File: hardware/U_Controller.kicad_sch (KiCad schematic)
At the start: 21 parts, among them J7001 Conn_01x06_Pin, J7002 Conn_ARM_JTAG_SWD_10, J7003 USB_C_Receptacle_USB2.0_16P, SW7001 SW_Wuerth_450301014042, U7001 STM32F401RBTx, U7003 USBLC6-2SC6, Y7001 Crystal_GND24

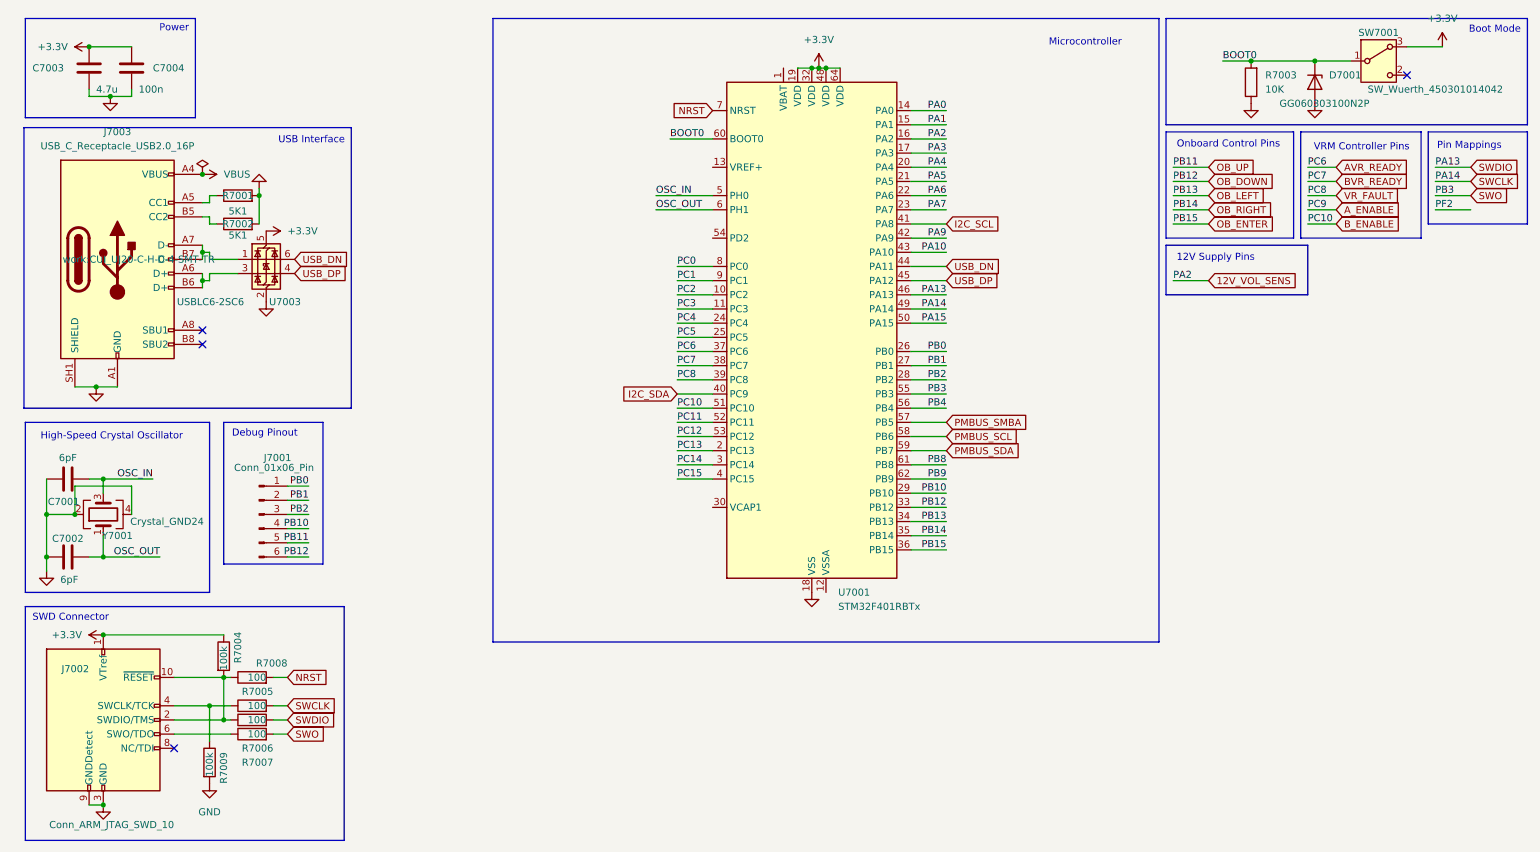
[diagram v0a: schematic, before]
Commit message: feat(schematic): refactor main heirarchy
This commit makes a bunch of changes to how power is delivered on the
schematic. It also adds the probit header and the i2c output connector
on the main page of the schematic. Lastly, it changes it so that USB
power should work and also not power the 5V rail to the mosfet ICs.
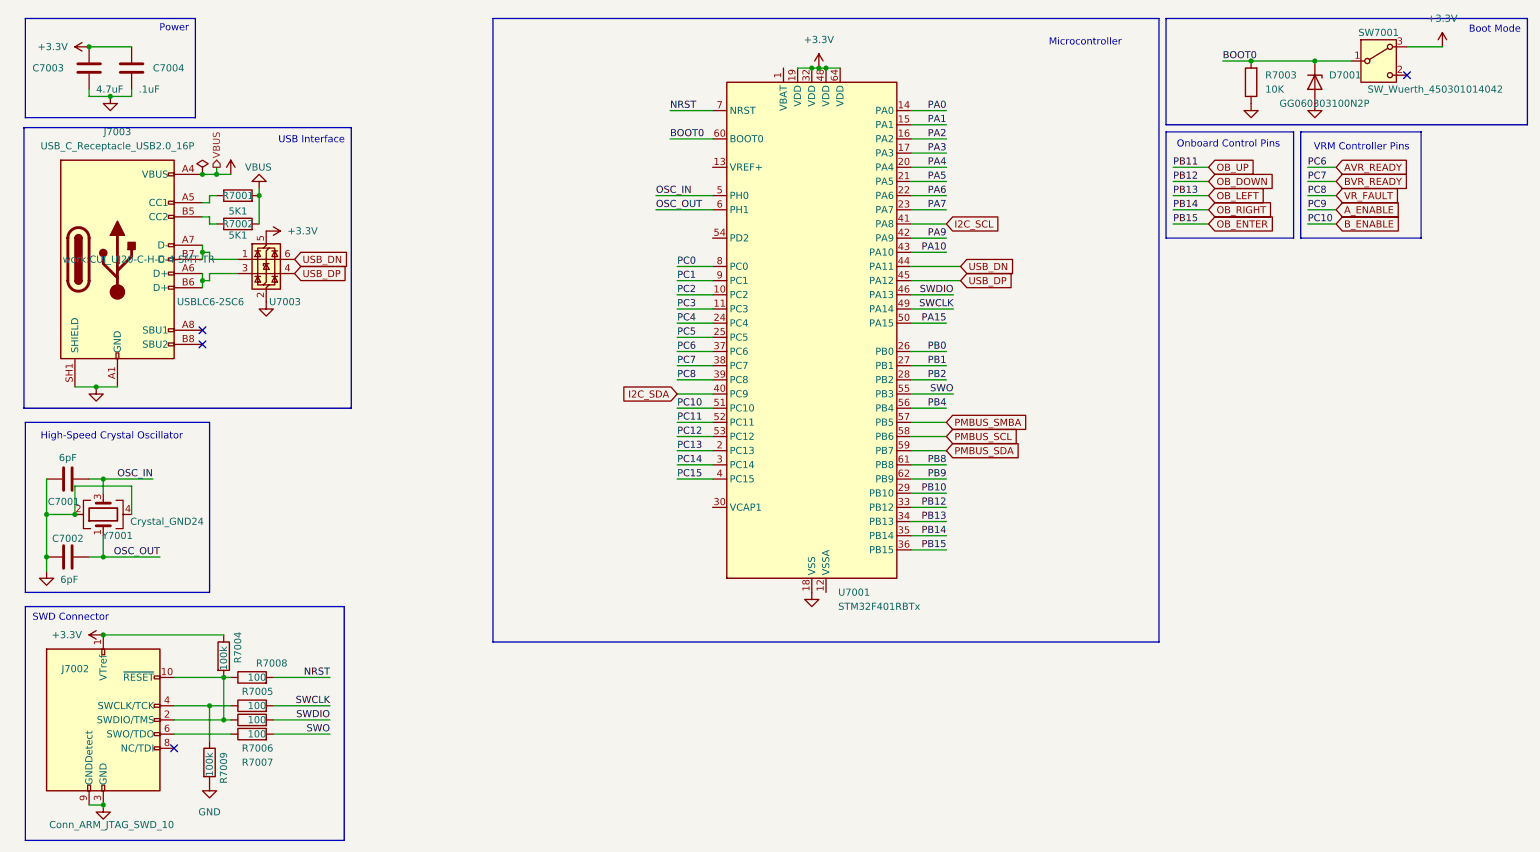
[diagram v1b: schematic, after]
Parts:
- removed J7001: Conn_01x06_Pin, symbol Connector:Conn_01x06_Pin
- C7003: value 4.7u -> 4.7uF
- C7004: value 100n -> .1uF
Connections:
- net 12V_VOL_SENS renamed PA2
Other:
- note removed: "12V Supply Pins"
- note removed: "Debug Pinout"
- note removed: "Pin Mappings"

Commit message: feat(schematic): added cooler mounting holes
added cooler mounting holes to schematic
changed temp pins to read proper tempurature
small fixes
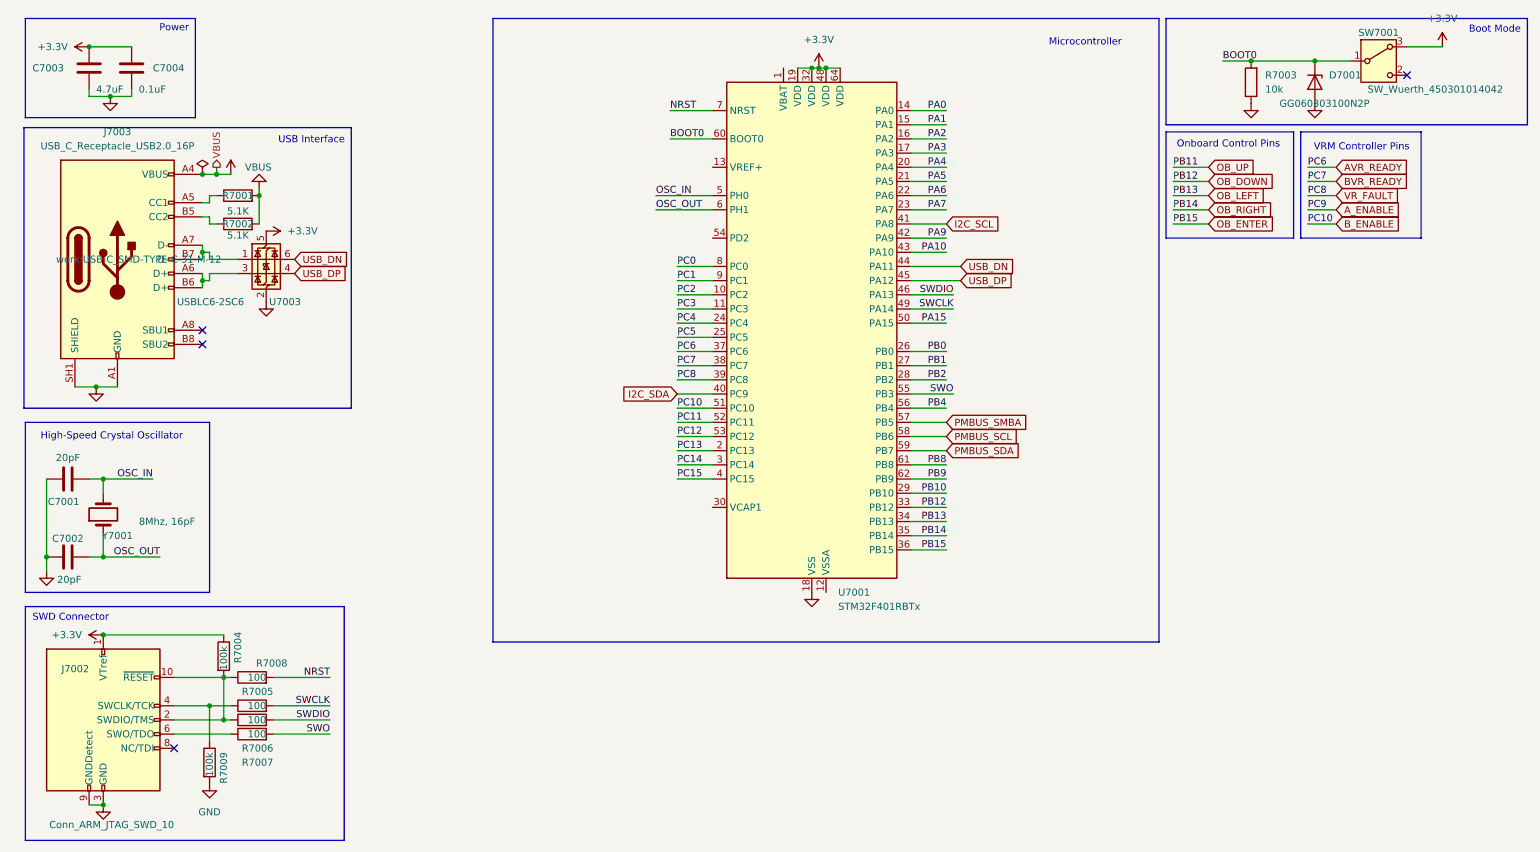
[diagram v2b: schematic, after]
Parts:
- C7001, C7002: value 6pF -> 20pF; footprint Capacitor_SMD:C_0805_2012Metric -> Capacitor_SMD:C_0402_1005Metric
- C7003: footprint Capacitor_SMD:C_0805_2012Metric -> Capacitor_SMD:C_0402_1005Metric
- C7004: value .1uF -> 0.1uF; footprint Capacitor_SMD:C_0805_2012Metric -> Capacitor_SMD:C_0402_1005Metric
- J7003: footprint work:CUI_UJ20-C-H-C-4-SMT-TR -> work:USB-C_SMD-TYPE-C-31-M-12
- R7001, R7002: value 5K1 -> 5.1K; footprint Resistor_SMD:R_0805_2012Metric -> Resistor_SMD:R_0402_1005Metric
- R7003: value 10K -> 10k; footprint Resistor_SMD:R_0805_2012Metric -> Resistor_SMD:R_0201_0603Metric
- R7004, R7005, R7006, R7007, R7008, R7009: footprint Resistor_SMD:R_0805_2012Metric -> Resistor_SMD:R_0402_1005Metric
- SW7001: footprint Button_Switch_THT:SW_Slide-03_Wuerth-WS-SLTV_10x2.5x6.4_P2.54mm -> work:SW-SMD_K3-1280S-K1
- Y7001: value Crystal_GND24 -> 8Mhz, 16pF; footprint Crystal:Crystal_SMD_Abracon_ABM10-4Pin_2.5x2.0mm -> Crystal:Crystal_SMD_HC49-SD_HandSoldering; symbol Device:Crystal_GND24 -> Device:Crystal
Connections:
- net GND: no longer Y7001.2, Y7001.4
- net OSC_IN: now also Y7001.2; no longer Y7001.3
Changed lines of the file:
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@@
 	)
 	(junction
-		(at 17.78 102.87)
-		(diameter 0)
-		(color 0 0 0 0)
-	)
-	(junction
-		(at 22.86 102.87)
-		(diameter 0)
-		(color 0 0 0 0)
-	)
-	(junction
 		(at 48.26 41.91)
 		(diameter 0)
@@
 	(wire
 		(pts
-			(xy 17.78 102.87) (xy 22.86 102.87)
-		)
-		(stroke
-			(width 0)
-			(type default)
-		)
-	)
-	(wire
-		(pts
-			(xy 33.02 97.79) (xy 22.86 97.79)
-		)
-		(stroke
-			(width 0)
-			(type default)
-		)
-	)
-	(wire
-		(pts
 			(xy 27.94 96.52) (xy 27.94 99.06)
 		)
@@
 	(wire
 		(pts
-			(xy 33.02 102.87) (xy 33.02 97.79)
-		)
-		(stroke
-			(width 0)
-			(type default)
-		)
-	)
-	(wire
-		(pts
 			(xy 219.71 43.18) (xy 226.06 43.18)
 		)
@@
 	(wire
 		(pts
-			(xy 17.78 96.52) (xy 17.78 102.87)
+			(xy 17.78 96.52) (xy 17.78 110.49)
 		)
 		(stroke
@@
 	(wire
 		(pts
-			(xy 17.78 102.87) (xy 17.78 110.49)
-		)
-		(stroke
-			(width 0)
-			(type default)
-		)
-	)
-	(wire
-		(pts
-			(xy 22.86 97.79) (xy 22.86 102.87)
-		)
-		(stroke
-			(width 0)
-			(type default)
-		)
-	)
-	(wire
-		(pts
 			(xy 130.81 66.04) (xy 137.16 66.04)
 		)
@@
 	)
 	(symbol
-		(lib_id "Device:Crystal_GND24")
+		(lib_id "Device:Crystal")
 		(at 27.94 102.87 90)
 		(unit 1)
@@
 			)
 		)
-		(property "Value" "Crystal_GND24"
+		(property "Value" "8Mhz, 16pF"
 			(at 39.37 104.14 90)
 			(effects
@@
 			)
 		)
-		(property "Footprint" "Crystal:Crystal_SMD_Abracon_ABM10-4Pin_2.5x2.0mm"
+		(property "Footprint" "Crystal:Crystal_SMD_HC49-SD_HandSoldering"
 			(at 27.94 102.87 0)
 			(effects
@@
 			)
 		)
-		(property "Datasheet" "https://www.digikey.com/en/products/detail/abracon-llc/ABM10W-48-0000MHZ-7-D1X-T3/7172572"
+		(property "Datasheet" "~"
 			(at 27.94 102.87 0)
 			(effects
@@
 			)
 		)
-		(property "Description" "Four pin crystal, GND on pins 2 and 4"
+		(property "Description" "Two pin crystal"
 			(at 27.94 102.87 0)
 			(effects
@@
 		(pin "1"
 		)
-		(pin "3"
-		)
-		(pin "4"
-		)
 		(instances
 			(project ""
@@
 			)
 		)
-		(property "Value" "6pF"
+		(property "Value" "20pF"
 			(at 21.59 92.71 90)
 			(effects
@@
 			)
 		)
-		(property "Footprint" "Capacitor_SMD:C_0805_2012Metric"
+		(property "Footprint" "Capacitor_SMD:C_0402_1005Metric"
 			(at 25.4 95.5548 0)
 			(effects
@@
 			)
 		)
-		(property "Datasheet" "~"
+		(property "Datasheet" "https://jlcpcb.com/partdetail/1906-0402CG200J500NT/C1554"
 			(at 21.59 96.52 0)
 			(effects
@@
 			)
 		)
-		(property "Footprint" "Resistor_SMD:R_0805_2012Metric"
+		(property "Footprint" "Resistor_SMD:R_0402_1005Metric"
 			(at 54.61 144.018 90)
 			(effects
@@
 			)
 		)
-		(property "Datasheet" "~"
+		(property "Datasheet" "https://jlcpcb.com/partdetail/25819-0402WGF1000TCE/C25076"
 			(at 54.61 142.24 0)
 			(effects
@@
 			)
 		)
-		(property "Footprint" "Resistor_SMD:R_0805_2012Metric"
+		(property "Footprint" "Resistor_SMD:R_0402_1005Metric"
 			(at 54.61 138.938 90)
 			(effects
@@
 			)
 		)
-		(property "Datasheet" "~"
+		(property "Datasheet" "https://jlcpcb.com/partdetail/25819-0402WGF1000TCE/C25076"
 			(at 54.61 137.16 0)
 			(effects
@@
 			)
 		)
-		(property "Footprint" "Capacitor_SMD:C_0805_2012Metric"
+		(property "Footprint" "Capacitor_SMD:C_0402_1005Metric"
 			(at 26.3652 26.67 0)
 			(effects
@@
 			)
 		)
-		(property "Datasheet" "~"
+		(property "Datasheet" "https://jlcpcb.com/partdetail/24469-CL05A475MP5NRNC/C23733"
 			(at 25.4 22.86 0)
 			(effects
@@
 			)
 		)
-		(property "Footprint" "Resistor_SMD:R_0805_2012Metric"
+		(property "Footprint" "Resistor_SMD:R_0402_1005Metric"
 			(at 54.61 141.478 90)
 			(effects
@@
 			)
 		)
-		(property "Datasheet" "~"
+		(property "Datasheet" "https://jlcpcb.com/partdetail/25819-0402WGF1000TCE/C25076"
 			(at 54.61 139.7 0)
 			(effects
@@
 			)
 		)
-		(property "Value" "6pF"
+		(property "Value" "20pF"
 			(at 21.844 114.554 90)
 			(effects
@@
 			)
 		)
-		(property "Footprint" "Capacitor_SMD:C_0805_2012Metric"
+		(property "Footprint" "Capacitor_SMD:C_0402_1005Metric"
 			(at 25.4 109.5248 0)
 			(effects
@@
 			)
 		)
-		(property "Datasheet" "~"
+		(property "Datasheet" "https://jlcpcb.com/partdetail/1906-0402CG200J500NT/C1554"
 			(at 21.59 110.49 0)
 			(effects
@@
 			)
 		)
-		(property "Footprint" "Button_Switch_THT:SW_Slide-03_Wuerth-WS-SLTV_10x2.5x6.4_P2.54mm"
+		(property "Footprint" "work:SW-SMD_K3-1280S-K1"
 			(at 256.54 31.75 0)
 			(effects
@@
 			)
 		)
-		(property "Datasheet" "https://www.we-online.com/components/products/datasheet/450301014042.pdf"
+		(property "Datasheet" "https://jlcpcb.com/partdetail/Korean_HropartsElec-K3_1280SF1/C92658"
 			(at 256.54 29.21 0)
 			(effects
@@
 			)
 		)
-		(property "Value" "10K"
+		(property "Value" "10k"
 			(at 236.22 26.6699 0)
 			(effects
@@
 			)
 		)
-		(property "Footprint" "Resistor_SMD:R_0805_2012Metric"
+		(property "Footprint" "Resistor_SMD:R_0201_0603Metric"
 			(at 235.458 25.4 90)
 			(effects
@@
 			)
 		)
-		(property "Datasheet" "~"
+		(property "Datasheet" "https://jlcpcb.com/partdetail/LizElec-CR0201FH1002G/C100126"
 			(at 233.68 25.4 0)
 			(effects
@@
 			)
 		)
-		(property "Footprint" "Resistor_SMD:R_0805_2012Metric"
+		(property "Footprint" "Resistor_SMD:R_0402_1005Metric"
 			(at 45.212 147.32 90)
 			(effects
@@
 			)
 		)
-		(property "Datasheet" "~"
+		(property "Datasheet" "https://jlcpcb.com/partdetail/26484-0402WGF1003TCE/C25741"
 			(at 46.99 147.32 0)
 			(effects
@@
 			)
 		)
-		(property "Value" ".1uF"
+		(property "Value" "0.1uF"
 			(at 34.29 26.67 0)
 			(effects
@@
 			)
 		)
-		(property "Footprint" "Capacitor_SMD:C_0805_2012Metric"
+		(property "Footprint" "Capacitor_SMD:C_0402_1005Metric"
 			(at 33.9852 26.67 0)
 			(effects
@@
 			)
 		)
-		(property "Datasheet" "~"
+		(property "Datasheet" "https://jlcpcb.com/partdetail/1933-0402F104M500NT/C1581"
 			(at 33.02 22.86 0)
 			(effects
@@
 			)
 		)
-		(property "Value" "5K1"
+		(property "Value" "5.1K"
 			(at 52.07 52.832 90)
 			(effects
@@
 			)
 		)
-		(property "Footprint" "Resistor_SMD:R_0805_2012Metric"
+		(property "Footprint" "Resistor_SMD:R_0402_1005Metric"
 			(at 52.07 52.578 90)
 			(effects
@@
 			)
 		)
-		(property "Datasheet" "~"
+		(property "Datasheet" "https://jlcpcb.com/partdetail/26648-0402WGF5101TCE/C25905"
 			(at 52.07 50.8 0)
 			(effects
@@
 			)
 		)
-		(property "Datasheet" "https://www.st.com/resource/en/datasheet/stm32f401rb.pdf"
+		(property "Datasheet" "https://jlcpcb.com/partdetail/Stmicroelectronics-STM32F401RBT6/C75278https://jlcpcb.com/partdetail/Stmicroelectronics-STM32F401RBT6/C75278"
 			(at 154.94 71.12 0)
 			(effects
@@
 			)
 		)
-		(property "Value" "5K1"
+		(property "Value" "5.1K"
 			(at 52.07 48.514 90)
 			(effects
@@
 			)
 		)
-		(property "Footprint" "Resistor_SMD:R_0805_2012Metric"
+		(property "Footprint" "Resistor_SMD:R_0402_1005Metric"
 			(at 52.07 47.498 90)
 			(effects
@@
 			)
 		)
-		(property "Datasheet" "~"
+		(property "Datasheet" "https://jlcpcb.com/partdetail/26648-0402WGF5101TCE/C25905"
 			(at 52.07 45.72 0)
 			(effects
@@
 			)
 		)
-		(property "Datasheet" "https://www.st.com/resource/en/datasheet/usblc6-2.pdf"
+		(property "Datasheet" "https://jlcpcb.com/partdetail/2790619-USBLC62SC6/C2687116"
 			(at 58.42 65.405 0)
 			(effects
@@
 			)
 		)
-		(property "Footprint" "Resistor_SMD:R_0805_2012Metric"
+		(property "Footprint" "Resistor_SMD:R_0402_1005Metric"
 			(at 54.61 133.858 90)
 			(effects
@@
 			)
 		)
-		(property "Datasheet" "~"
+		(property "Datasheet" "https://jlcpcb.com/partdetail/25819-0402WGF1000TCE/C25076"
 			(at 54.61 132.08 0)
 			(effects
@@
 			)
 		)
-		(property "Footprint" "work:CUI_UJ20-C-H-C-4-SMT-TR"
+		(property "Footprint" "work:USB-C_SMD-TYPE-C-31-M-12"
 			(at 34.29 57.15 0)
 			(effects
@@
 			)
 		)
-		(property "Datasheet" "https://www.digikey.com/en/products/detail/cnc-tech/3221-10-0100-00/4878932"
+		(property "Datasheet" "https://jlcpcb.com/partdetail/Hanxia-HX_JN1_27_2x5_TP_H49/C42372555"
 			(at 19.05 171.45 90)
 			(effects
@@
 			)
 		)
-		(property "Footprint" "Resistor_SMD:R_0805_2012Metric"
+		(property "Footprint" "Resistor_SMD:R_0402_1005Metric"
 			(at 47.752 128.27 90)
 			(effects
@@
 			)
 		)
-		(property "Datasheet" "~"
+		(property "Datasheet" "https://jlcpcb.com/partdetail/26484-0402WGF1003TCE/C25741"
 			(at 49.53 128.27 0)
 			(effects

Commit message: feat(hardware): microcontroller routing
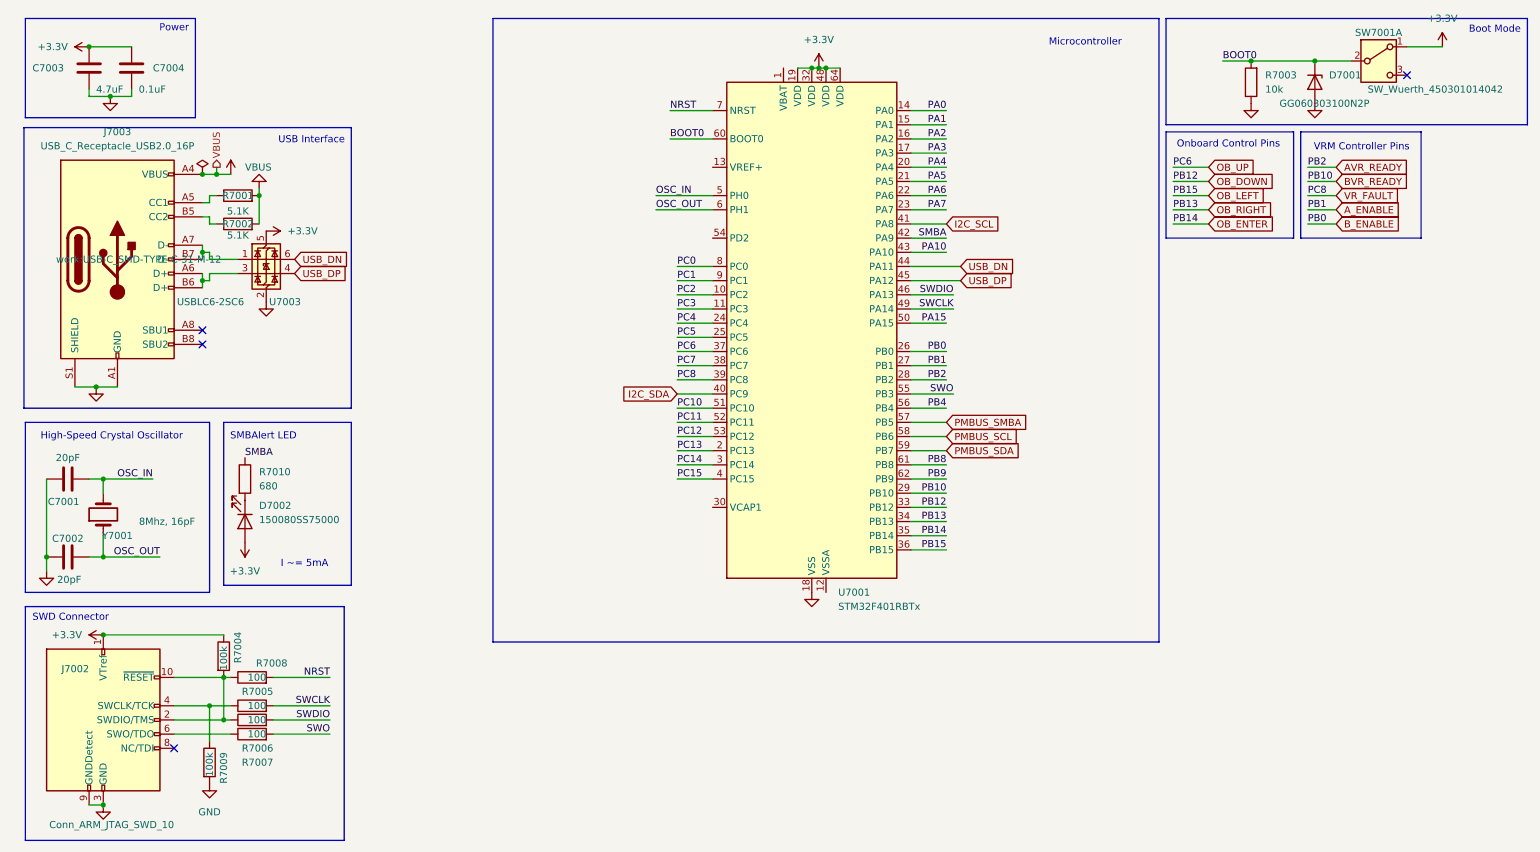
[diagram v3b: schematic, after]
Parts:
- added D7002: 150080SS75000, LED_SMD:LED_0603_1608Metric, symbol Device:LED
- added R7010: 680, Resistor_SMD:R_0805_2012Metric, symbol Device:R
- SW7001: symbol Switch:SW_Wuerth_450301014042 -> Switch:SW_DPDT_x2
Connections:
- net PB0 is gone; now on net B_ENABLE: U7001.26 (PB0)
- net PB1 is gone; now on net A_ENABLE: U7001.27 (PB1)
- net PB10 is gone; now on net BVR_READY: U7001.29 (PB10)
- net PB2 is gone; now on net AVR_READY: U7001.28 (PB2)
- net +3.3V: now also SW7001.1 (A), D7002.2 (A); no longer SW7001.3 (A)
- net AVR_READY: no longer U7001.37 (PC6)
- net BOOT0: now also SW7001.2 (B); no longer SW7001.1 (B)
- net BVR_READY: no longer U7001.38 (PC7)
- net B_ENABLE: no longer U7001.51 (PC10)
- net GND: now also J7003.A12 (GND), J7003.B12 (GND), J7003.S1 (SHIELD); no longer J7003.SH1 (SHIELD), J7003.SH2 (SHIELD), J7003.SH3 (SHIELD), J7003.SH4 (SHIELD)
- net OB_ENTER: now also U7001.35 (PB14); no longer U7001.36 (PB15)
- net OB_LEFT: now also U7001.36 (PB15); no longer U7001.34 (PB13)
- net OB_RIGHT: now also U7001.34 (PB13); no longer U7001.35 (PB14)
- net OB_UP: now also U7001.37 (PC6)
- net VBUS: now also J7003.A9 (VBUS), J7003.B9 (VBUS)
- net PA9 renamed SMBA
- net SMBA: now also R7010.1
- new net: D7002.1 (K), R7010.2
- new net PC10: U7001.51 (PC10)
- new net PC7: U7001.38 (PC7)
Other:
- note added: "I ~= 5mA"
- note added: "SMBAlert LED"
